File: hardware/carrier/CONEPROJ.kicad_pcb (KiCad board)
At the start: 4 copper layers, 86 x 50.5 mm, 68 parts, among them J2 Conn_02x15_Odd_Even_Shielded, J304 U.FL-R-SMT-1(10), J4 DTM1312PA12PBR008, J5 TC2030-IDC, Q2 Q_Dual_NMOS_S1G1S2G2D2D2D1D1, Q3 Q_Dual_NMOS_S1G1S2G2D2D2D1D1, Q4 Q_Dual_NMOS_S1G1S2G2D2D2D1D1, Q5 Q_Dual_NMOS_S1G1S2G2D2D2D1D1, Q6 Q_Dual_NMOS_S1G1S2G2D2D2D1D1, Q7 Q_Dual_NMOS_S1G1S2G2D2D2D1D1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

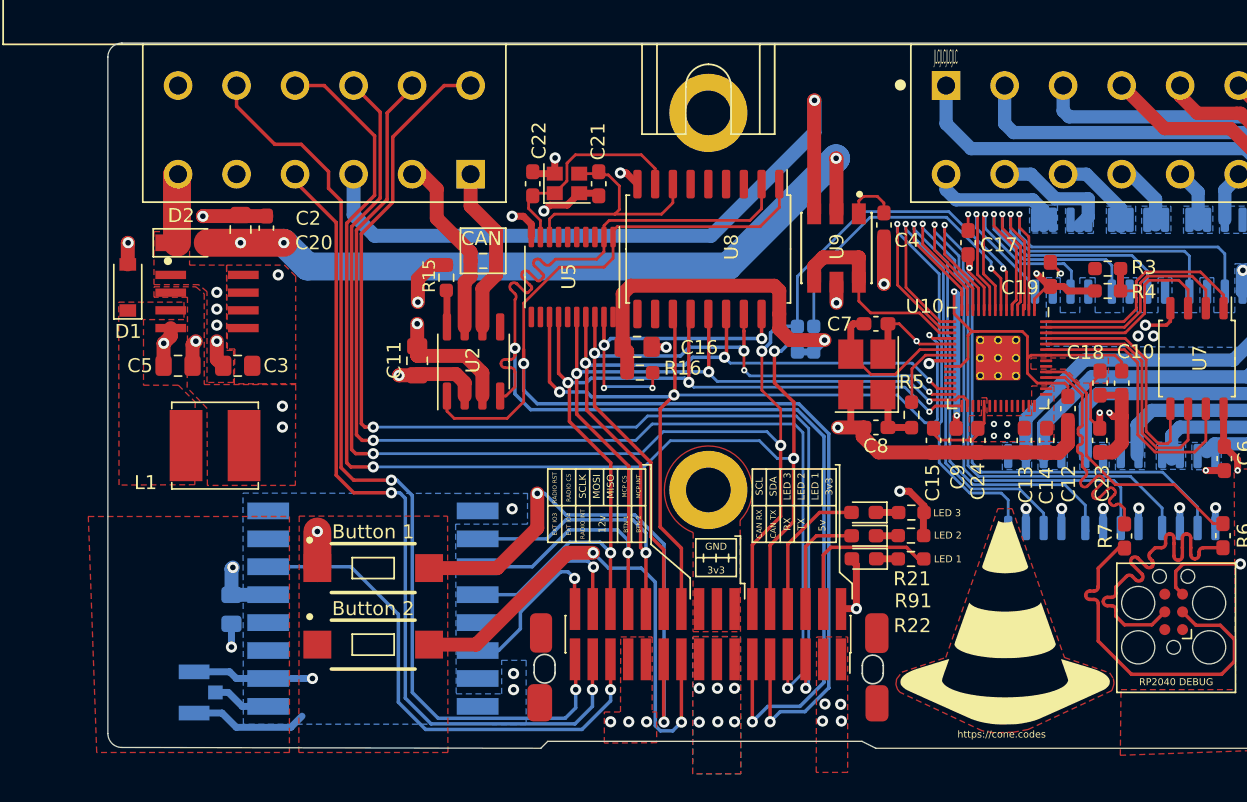
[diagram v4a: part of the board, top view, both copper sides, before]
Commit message: Add 3v3 regulator for carrier board
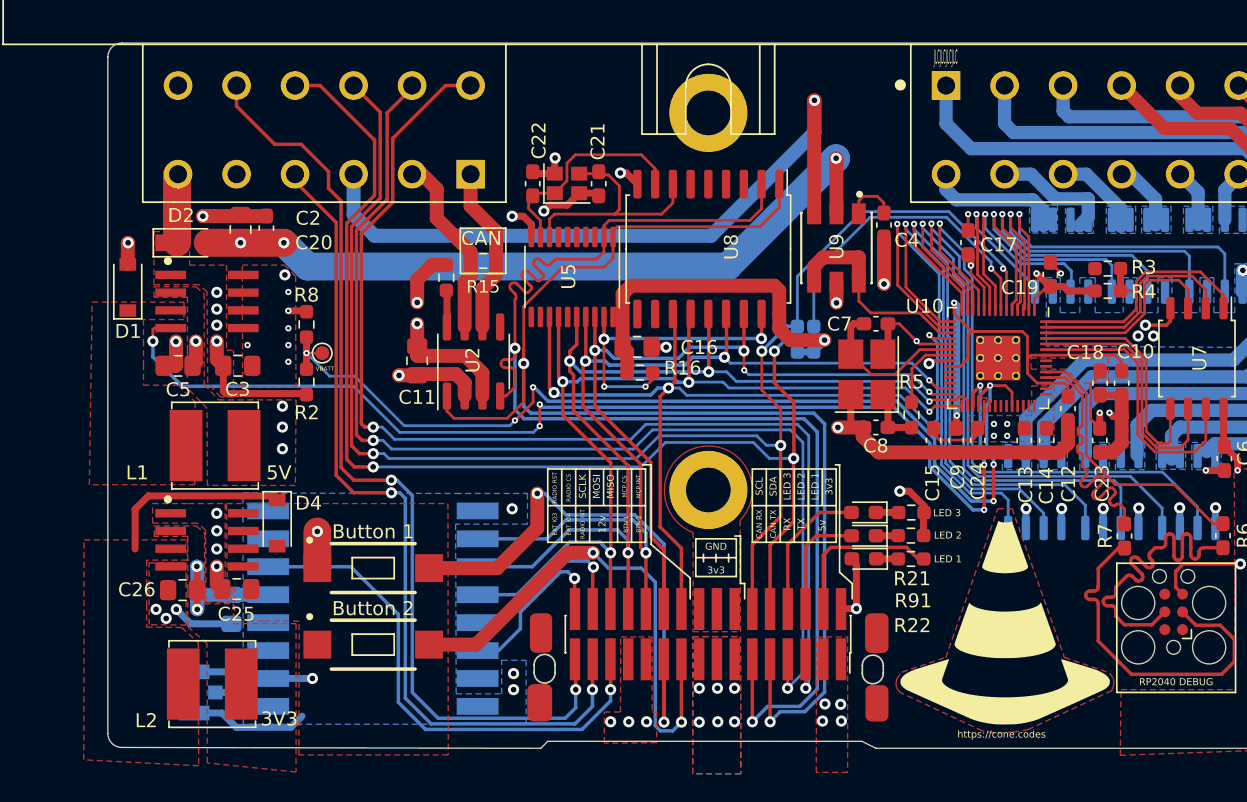
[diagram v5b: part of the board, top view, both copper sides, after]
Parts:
- added C25: 10uF, Capacitor_SMD:C_0805_2012Metric_Pad1.18x1.45mm_HandSolder, F.Cu at (33.2, 81.1)
- added C26: 10uF, Capacitor_SMD:C_0805_2012Metric_Pad1.18x1.45mm_HandSolder, F.Cu at (29.4, 81.2)
- added D4: D_Small, Diode_SMD:D_SOD-123, F.Cu at (36.1, 76.4)
- added L2: 6.8uH, Inductor_SMD:L_Bourns_SRN6045TA, F.Cu at (31.5, 87.9)
- added R2: 10k, Resistor_SMD:R_0603_1608Metric_Pad0.98x0.95mm_HandSolder, F.Cu at (38.2, 66.3)
- added R8: 10k, Resistor_SMD:R_0603_1608Metric_Pad0.98x0.95mm_HandSolder, F.Cu at (38.2, 62.1)
- added TP2: vbat_sense, TestPoint:TestPoint_Pad_D1.0mm, F.Cu at (39.4, 64.2)
- added U3: AP1509, AP1509-50SG-13:SO08, F.Cu at (31.1, 77.6)
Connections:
- U10 pad 12: /GPO_12 -> /GPO_5
- U10 pad 31: unconnected-(U10-Pad31) -> /5V_EN
- U10 pad 32: unconnected-(U10-Pad32) -> /VBAT_SENSE
- U10 pad 38: unconnected-(U10-Pad38) -> /VBAT_SENSE
- U304 pad 4: GND -> /5V_EN
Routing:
- net /5V_EN: track 0.00 -> 81.6 mm, vias 0 -> 6
- net /VBAT_SENSE: track 0.00 -> 74.1 mm, vias 0 -> 6
- net /GPO_5: track 0.00 -> 42.4 mm, vias 0 -> 1
- net /GPO_12: track 42.1 -> 0.00 mm, vias 1 -> 0
- net Net-(D4-Pad1): track 0.00 -> 13.5 mm
- net /EXT_12V: track 56.3 -> 69.6 mm, vias 7 -> 11
- net +3V3: track 75.8 -> 82.1 mm, vias 19 -> 20
- net GND: track 123.5 -> 127.3 mm, vias 37 -> 45
- net +1V1: track 35.7 -> 34.1 mm
- net /MCP_RESET: track 25.4 -> 24.2 mm
- net /EXT_SPI_MOSI: track 69.4 -> 70.5 mm
- net /EXT_IO3: track 64.0 -> 64.6 mm
- net /EXT_I2C_SCL: track 108.0 -> 107.5 mm
- net /CAN_TX: track 91.2 -> 91.7 mm
- net +5V: vias 7 -> 8
- added copper zone on F.Cu, net Net-(D4-Pad1)
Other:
- board text added: "3V3"
- board text added: "VBATT"

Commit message: Add motor controller for popups or whatever
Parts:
- removed Q3, Q4: Q_Dual_NMOS_S1G1S2G2D2D2D1D1, Package_SO:SO-8_3.9x4.9mm_P1.27mm
- added C27: 470nf, Capacitor_SMD:C_0805_2012Metric_Pad1.18x1.45mm_HandSolder, F.Cu at (118.5, 83.0)
- added C28: 10nf, Capacitor_SMD:C_0805_2012Metric_Pad1.18x1.45mm_HandSolder, F.Cu at (122.6, 76.2)
- added C29: 100nf, Capacitor_SMD:C_0805_2012Metric_Pad1.18x1.45mm_HandSolder, F.Cu at (113.7, 83.0)
- added C30: 100nf, Capacitor_SMD:C_0805_2012Metric_Pad1.18x1.45mm_HandSolder, F.Cu at (122.6, 79.2)
- added C31: 10uf, Capacitor_SMD:CP_Elec_5x5.9, F.Cu at (115.7, 78.1)
- added U4: DRV8844PWP, DRV8844PWP:IC_TPS61196PWPRQ1, B.Cu at (90.1, 78.3)
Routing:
- net /GPO_4: track 44.4 -> 27.9 mm
- net /GPO_5: track 42.4 -> 28.3 mm
- net /GPO_6: track 41.0 -> 27.4 mm
- net /GPO_3: track 38.6 -> 25.5 mm
- net /GPO_2: track 36.6 -> 27.0 mm
- net /GPO_1: track 35.8 -> 27.9 mm
- net /GPO_6_OUT: track 44.2 -> 48.3 mm
- net GND: track 127.3 -> 123.3 mm, vias 45 -> 41
- net /5V_EN: track 81.6 -> 78.6 mm
- net /GPO_3_OUT: track 54.5 -> 55.7 mm
- net /GPO_2_OUT: track 58.2 -> 58.9 mm
- net /GPO_1_OUT: track 60.6 -> 61.2 mm

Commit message: Finish motor driver
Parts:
- removed Q6: Q_Dual_NMOS_S1G1S2G2D2D2D1D1, Package_SO:SO-8_3.9x4.9mm_P1.27mm
- C28: value 10nf -> 0.01uf
- C29: value 100nf -> 0.1uf
- C30: value 100nf -> 10uf
- G***: moved to B.Cu
- moved G*** 57.4 mm to (33.7, 65.7), turned to 180 degrees
- moved C28 38.6 mm to (84.0, 75.5), turned to -90 degrees
- moved C31 27.6 mm to (88.4, 82.1)
- moved C30 26.1 mm to (96.8, 75.0)
- moved C29 25.1 mm to (90.8, 72.9)
- moved C27 24.5 mm to (94.2, 86.8), turned to 180 degrees
- moved U4 0.80 mm to (90.9, 78.3)
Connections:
- net /GPO_1_OUT renamed /MOTOR1_OUT1
- net /GPO_2_OUT renamed /MOTOR1_OUT2
- net /GPO_3_OUT renamed /MOTOR2_OUT1
- net Net-(C28-Pad1) renamed /CP1
- C28 pad 2: Net-(C28-Pad2) -> /CP2
- J4 pad A4: /GPO_4_OUT -> /MOTOR2_OUT2
- U10 pad 34: unconnected-(U10-Pad34) -> /GPO_11
- U10 pad 35: unconnected-(U10-Pad35) -> /GPO_10
- U10 pad 36: unconnected-(U10-Pad36) -> /DRV_SLEEP
- U10 pad 37: unconnected-(U10-Pad37) -> /MCP_RESET
- U4 pad 10: /GPO_6_OUT -> /MOTOR2_OUT2
- U4 pad 12: (no net) -> unconnected-(U4-Pad12)
- U4 pad 13: (no net) -> unconnected-(U4-Pad13)
- U4 pad 17: unconnected-(U4-Pad17) -> /DRV_SLEEP
- U4 pad 2: GND -> /CP2
- U4 pad 20: unconnected-(U4-Pad20) -> /GPO_4
- U4 pad 21: unconnected-(U4-Pad21) -> /GPO_11
- U4 pad 22: unconnected-(U4-Pad22) -> /GPO_3
- U4 pad 23: unconnected-(U4-Pad23) -> /GPO_10
- U4 pad 24: unconnected-(U4-Pad24) -> /GPO_2
- U4 pad 25: unconnected-(U4-Pad25) -> /GPO_6
- U4 pad 26: unconnected-(U4-Pad26) -> /GPO_1
- U4 pad 27: unconnected-(U4-Pad27) -> /GPO_5
- U4 pad 28: (no net) -> GND
- U4 pad 30: (no net) -> GND
- U4 pad 31: (no net) -> GND
- U4 pad 32: (no net) -> GND
- U4 pad 33: (no net) -> GND
- U4 pad 34: (no net) -> GND
- U4 pad 35: (no net) -> GND
- U4 pad 36: (no net) -> GND
- U4 pad 37: (no net) -> GND
- U4 pad 38: (no net) -> GND
- U4 pad 39: (no net) -> GND
- U4 pad 40: (no net) -> GND
- U4 pad 41: (no net) -> GND
- U4 pad 42: (no net) -> GND
- U4 pad 43: (no net) -> GND
- U4 pad 44: (no net) -> GND
- U4 pad 45: (no net) -> GND
- U4 pad 46: (no net) -> GND
- U4 pad 47: (no net) -> GND
- U4 pad 48: (no net) -> GND
- U4 pad 49: (no net) -> GND
- U4 pad 50: (no net) -> GND
- U4 pad 6: unconnected-(U4-Pad6) -> GND
- U4 pad 9: unconnected-(U4-Pad9) -> GND
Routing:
- net /GPO_6_OUT: track 48.3 -> 0.00 mm, vias 1 -> 0
- net /MOTOR2_OUT2: track 0.00 -> 47.7 mm, vias 0 -> 1
- net /GPO_5_OUT: track 42.2 -> 0.00 mm, vias 1 -> 0
- net /GPO_4_OUT: track 38.1 -> 0.00 mm, vias 1 -> 0
- net /DRV_SLEEP: track 0.00 -> 36.8 mm, vias 0 -> 3
- net /GPO_11: track 0.00 -> 33.9 mm, vias 0 -> 3
- net /MCP_RESET: track 24.2 -> 54.2 mm
- net /GPO_10: track 0.00 -> 28.4 mm, vias 0 -> 3
- net /GPO_2: track 27.0 -> 54.2 mm, vias 1 -> 3
- net /GPO_4: track 27.9 -> 53.9 mm, vias 1 -> 3
- net /GPO_3: track 25.5 -> 51.1 mm, vias 1 -> 3
- net Net-(C29-Pad2): track 0.00 -> 21.7 mm, vias 0 -> 2
- net /GPO_1: track 27.9 -> 49.2 mm, vias 1 -> 3
- net /GPO_6: track 27.4 -> 45.1 mm, vias 1 -> 3
- net /GPO_5: track 28.3 -> 45.7 mm, vias 1 -> 3
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- added copper zone on B.Cu, net (none)
- added copper zone on B.Cu, net /MOTOR2_OUT2
- added copper zone on In2.Cu, net GND
- added copper zone on F.Cu, net Net-(C29-Pad2)
- removed copper zone on B.Cu, net /GPO_4_OUT
- removed copper zone on B.Cu, net /GPO_5_OUT
- removed copper zone on B.Cu, net /GPO_6_OUT
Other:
- board text added: "BLU"
- board text added: "GRN"
- board text added: "M1 1"
- board text added: "M1 2"
- board text added: "M2 1"
- board text added: "M2 2"
- board text added: "RED"
- board text removed: "GPO1"
- board text removed: "GPO2"
- board text removed: "GPO3"
- board text removed: "GPO4"
- board text removed: "GPO5"
- board text removed: "GPO6"
- board text removed: "GPOB"
- board text removed: "GPOG"
- board text removed: "GPOR"

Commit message: Finish motor controller
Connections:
- net /GPO_1 renamed /EN1
- net /GPO_2 renamed /EN2
- net /GPO_3 renamed /EN3
- net /GPO_4 renamed /EN4
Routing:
- net +3V3: track 83.5 -> 82.1 mm
- net /G_OUT: track 8.94 -> 7.69 mm
- net Net-(C7-Pad1): track 11.5 -> 12.0 mm
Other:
- board text added: "MOTOR CONTROL"
